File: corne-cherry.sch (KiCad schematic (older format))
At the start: 164 parts, among them J1 MJ-4PP-9, J2 OLED, J3 MJ-4PP-9, J4 OLED, SW1 SW_PUSH, SW10 SW_PUSH, SW11 SW_PUSH, SW12 SW_PUSH, SW13 SW_PUSH, SW14 SW_PUSH, SW15 SW_PUSH, SW16 SW_PUSH, SW17 SW_PUSH, SW18 SW_PUSH, SW19 SW_PUSH, SW2 SW_PUSH, SW20 SW_PUSH, SW21 SW_PUSH, SW22 SW_PUSH, SW23 SW_PUSH, SW24 SW_PUSH, SW25 SW_PUSH, SW26 SW_PUSH, SW27 SW_PUSH, SW28 SW_PUSH, SW29 SW_PUSH, SW3 SW_PUSH, SW30 SW_PUSH, SW31 SW_PUSH, SW32 SW_PUSH, SW33 SW_PUSH, SW34 SW_PUSH, SW35 SW_PUSH, SW36 SW_PUSH, SW37 SW_PUSH, SW38 SW_PUSH, SW39 SW_PUSH, SW4 SW_PUSH, SW40 SW_PUSH, SW41 SW_PUSH, SW42 SW_PUSH, SW43 SW_PUSH, SW44 SW_PUSH, SW45 SW_PUSH, SW46 SW_PUSH, SW47 SW_PUSH, SW48 SW_PUSH, SW5 SW_PUSH, SW6 SW_PUSH, SW7 SW_PUSH, SW8 SW_PUSH, SW9 SW_PUSH, U1 ProMicro, U2 ProMicro

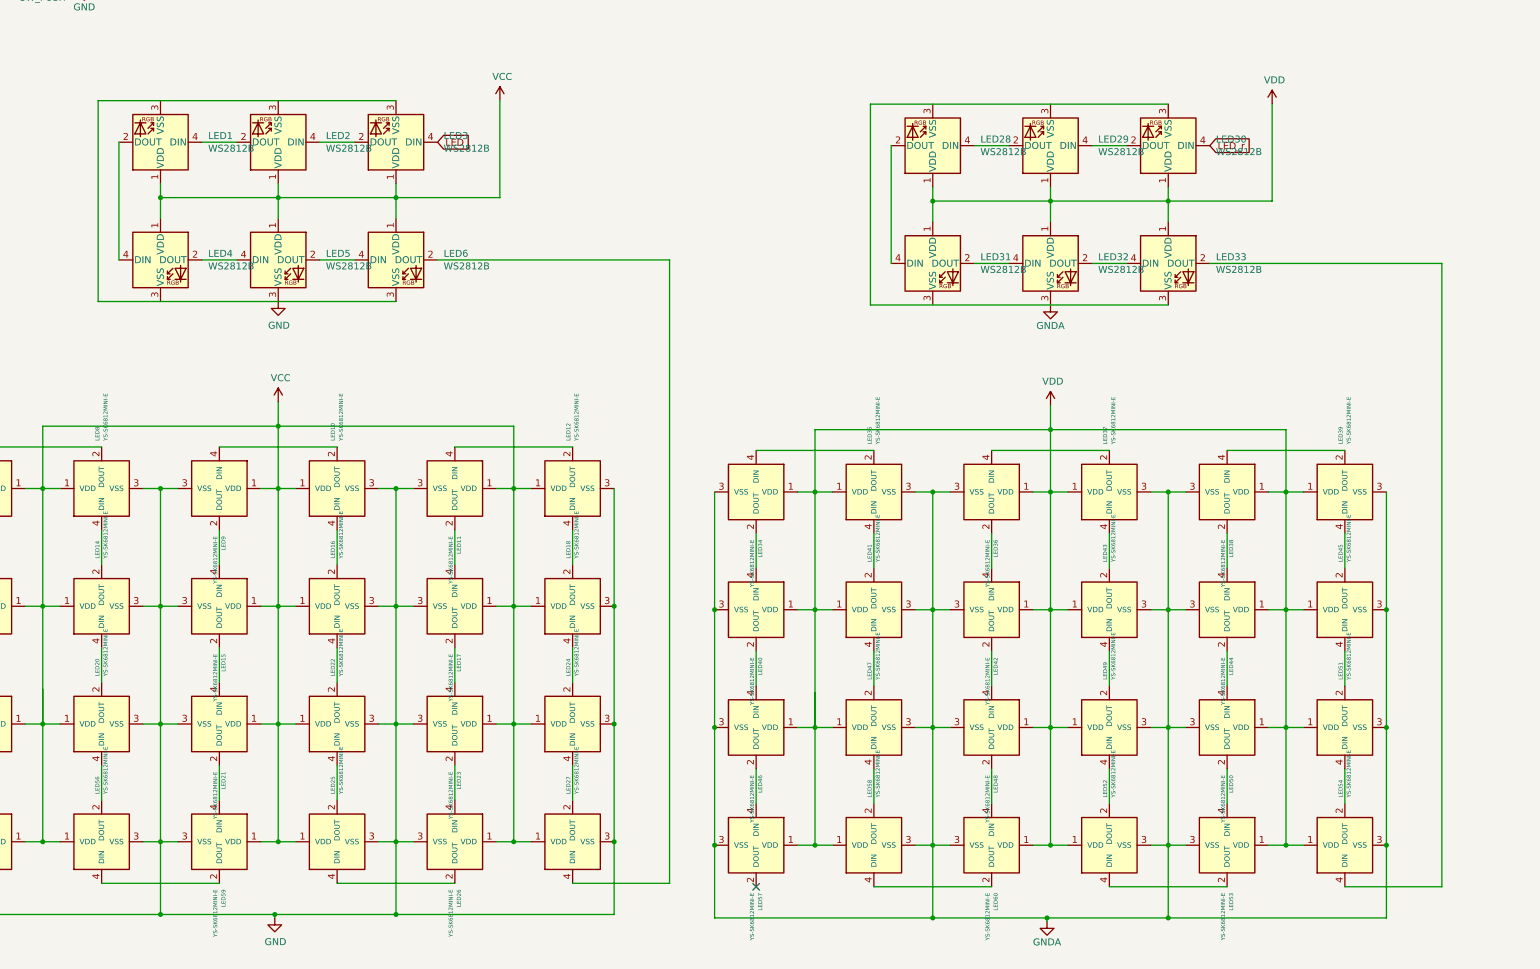
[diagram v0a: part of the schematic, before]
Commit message: updated schematic and pcb
schematic: fixed unconnected pins and aligned some components to the grid
pcb: updated wires according to new schematic, created outline (edge
cuts layer), added a few more labels, fixed a few smaller mistakes
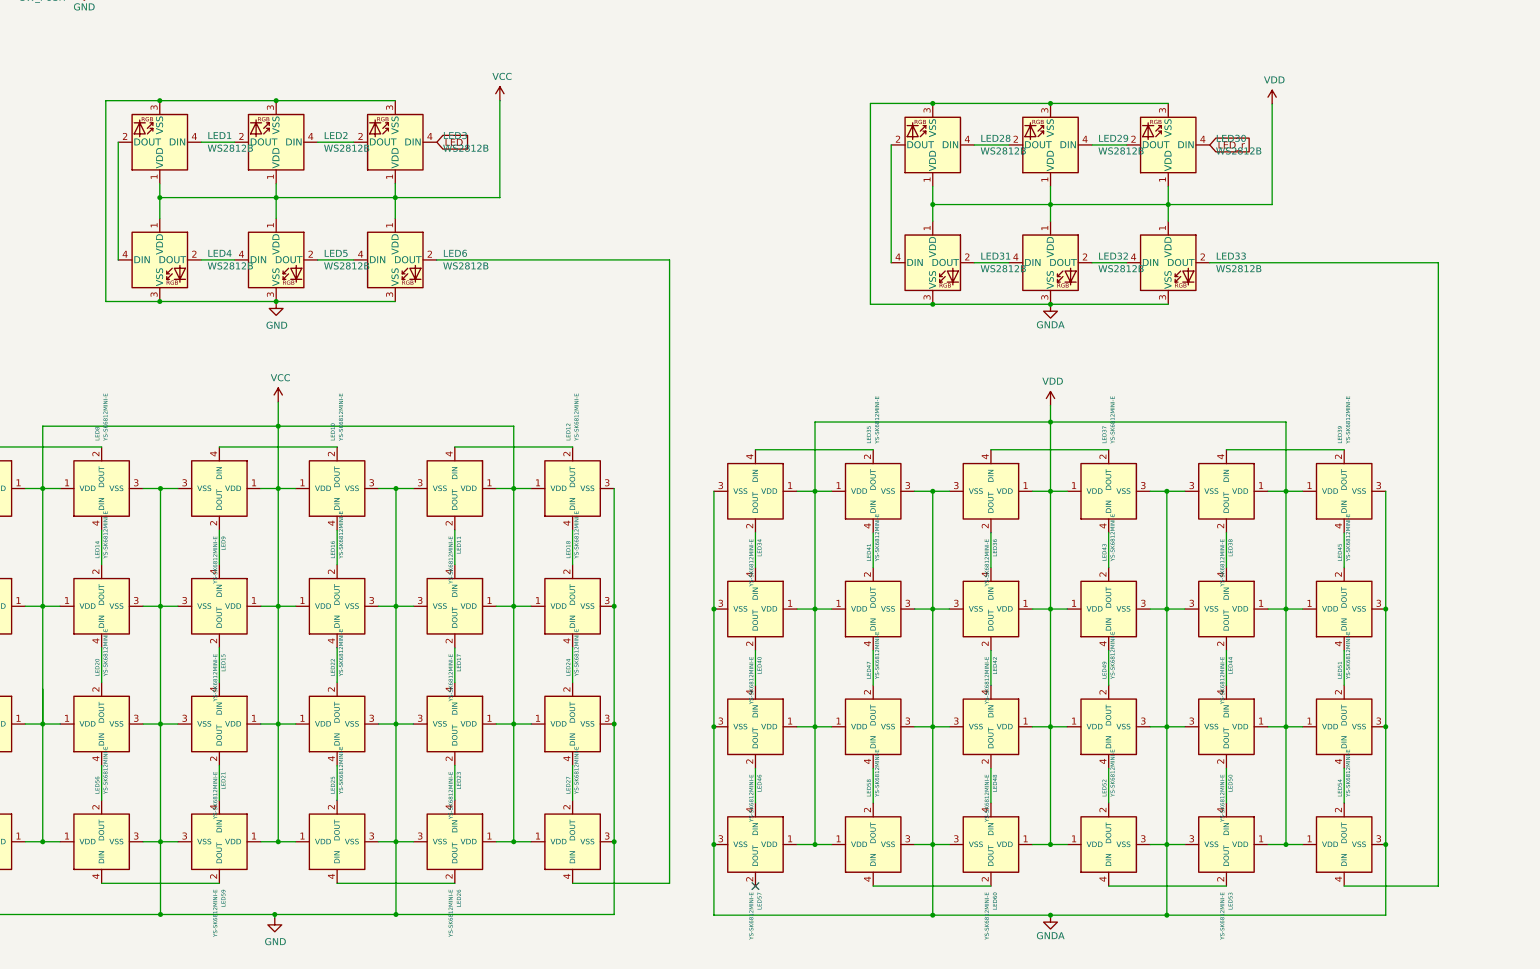
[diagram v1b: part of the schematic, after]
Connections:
- net GND: now also LED1.3 (VSS), LED2.3 (VSS), LED3.3 (VSS), LED4.3 (VSS), LED6.3 (VSS)
- net GNDA: now also LED28.3 (VSS), LED29.3 (VSS), LED30.3 (VSS), LED31.3 (VSS), LED33.3 (VSS)

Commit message: added zip of gerber files and assembly related files
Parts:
- D1, D10, D11, D12, D13, D14, D15, D16, D17, D18, D19, D2, D20, D21, D22, D23, D24, D25, D26, D27, D28, D29, D3, D30, D31, D32, D33, D34, D35, D36, D37, D38, D39, D4, D40, D41, D42, D43, D44, D45, D46, D47, D48, D5, D6, D7, D8, D9: LCSC Part # (none) -> C81598
- LED1, LED2, LED28, LED29, LED3, LED30, LED31, LED32, LED33, LED4, LED5, LED6: LCSC Part # (none) -> C114586
